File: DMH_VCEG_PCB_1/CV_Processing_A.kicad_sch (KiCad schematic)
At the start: 57 parts, among them Q1 BC558, Q2 BC558, Q3 BC548, Q4 BC548, Q5 BC548, Q6 BC548, U10 TL074, U8 TL074, U9 TL074

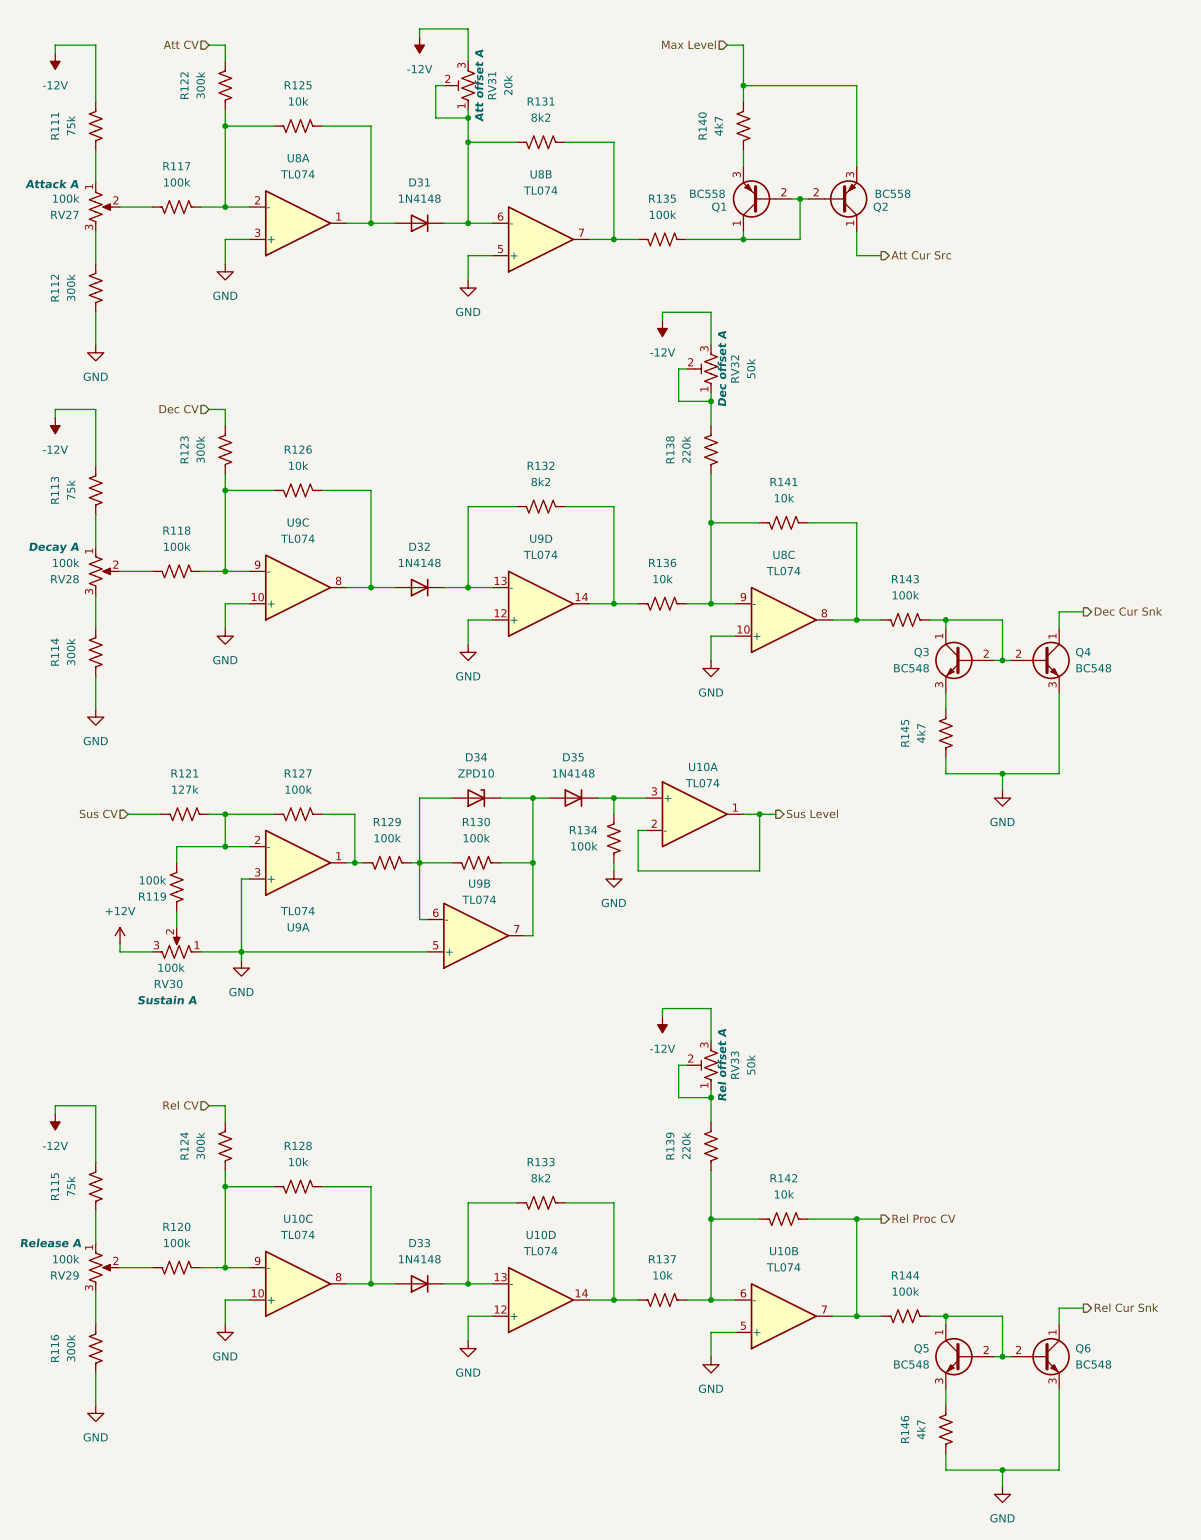
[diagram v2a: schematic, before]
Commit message: Re-annotated whole circuit
Now need to place interface pins and determine in and out of board settings
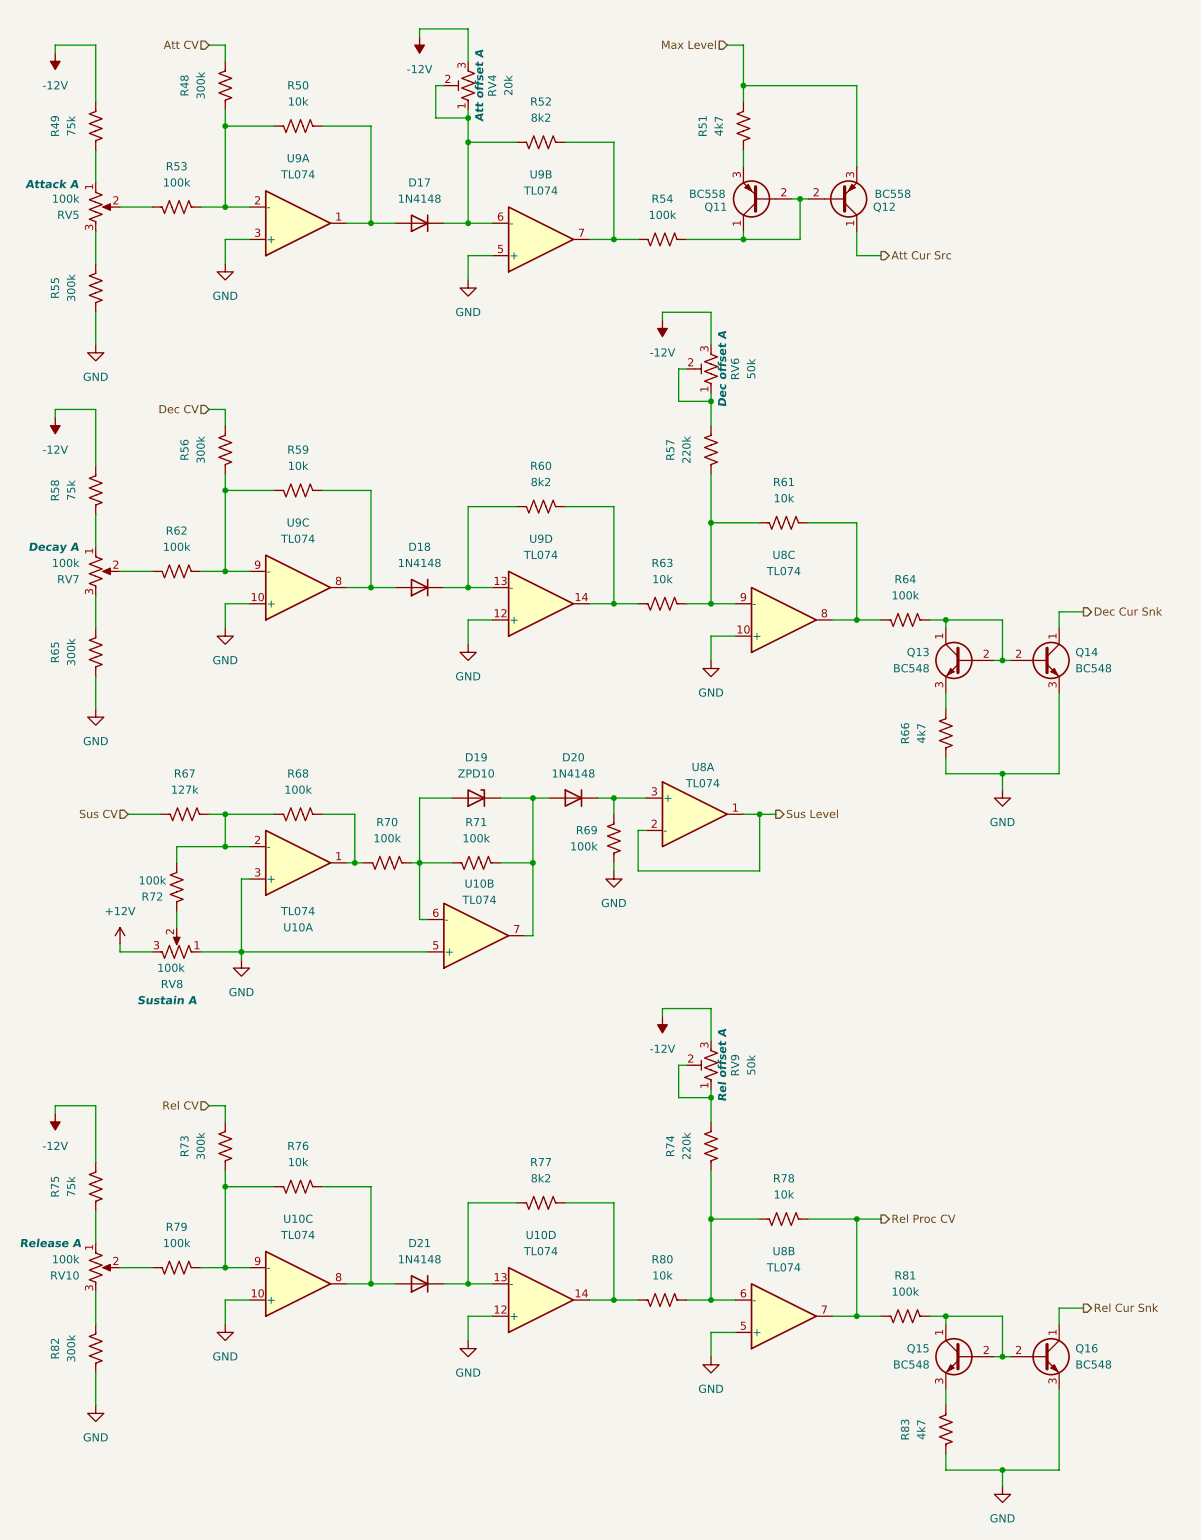
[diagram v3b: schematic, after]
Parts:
- renumbered D31 to D17, D32 to D18, D34 to D19, D35 to D20, D33 to D21, Q1 to Q11, Q2 to Q12, Q3 to Q13, Q4 to Q14, Q5 to Q15, Q6 to Q16, R122 to R48, R111 to R49, R125 to R50, R140 to R51, R131 to R52, R117 to R53, R135 to R54, R112 to R55, R123 to R56, R138 to R57, R113 to R58, R126 to R59, R132 to R60, R141 to R61, R118 to R62, R136 to R63, R143 to R64, R114 to R65, R145 to R66, R121 to R67, R127 to R68, R134 to R69, R129 to R70, R130 to R71, R119 to R72, R124 to R73, R139 to R74, R115 to R75, R128 to R76, R133 to R77, R142 to R78, R120 to R79, R137 to R80, R144 to R81, R116 to R82, R146 to R83, RV29 to RV10, RV31 to RV4, RV27 to RV5, RV32 to RV6, RV28 to RV7, RV30 to RV8, RV33 to RV9, U9 to U10, U10 to U8, U8 to U9

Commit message: Ready for breadboarding
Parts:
- added J22: Conn_01x10_PinHeader, Connector_PinHeader_2.54mm:PinHeader_1x10_P2.54mm_Vertical, symbol SynthStuff:Conn_01x10_PinHeader
- RV4, RV6, RV9: footprint Potentiometer_THT:Potentiometer_Bourns_3296W_Vertical -> Potentiometer_THT:Potentiometer_Bourns_3296X_Horizontal
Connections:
- net Att CV: now also J22.5 (Pin_5)
- net Dec CV: now also J22.6 (Pin_6)
- net Max Level: now also J22.4 (Pin_4)
- net Rel CV: now also J22.8 (Pin_8)
- net Sus CV: now also J22.7 (Pin_7)
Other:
- note added: "PCB 2"

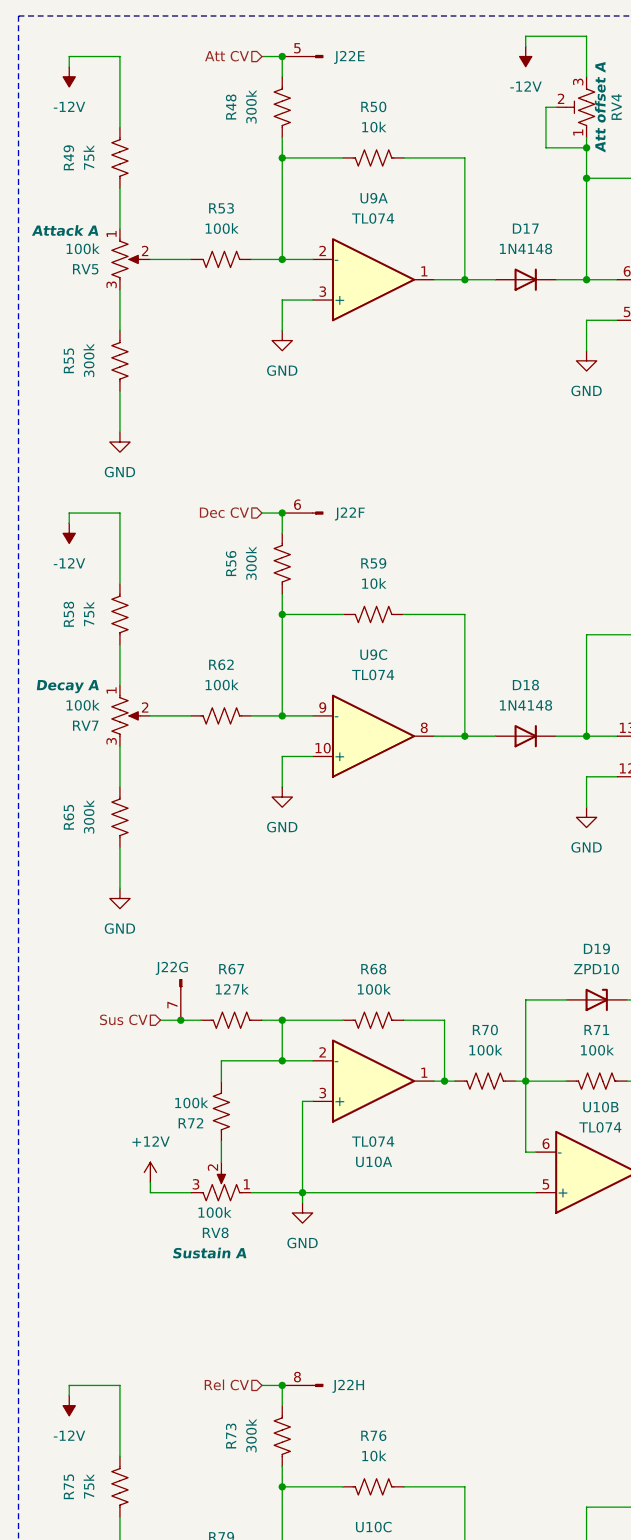
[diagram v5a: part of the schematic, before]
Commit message: PCB 2 placement in progress
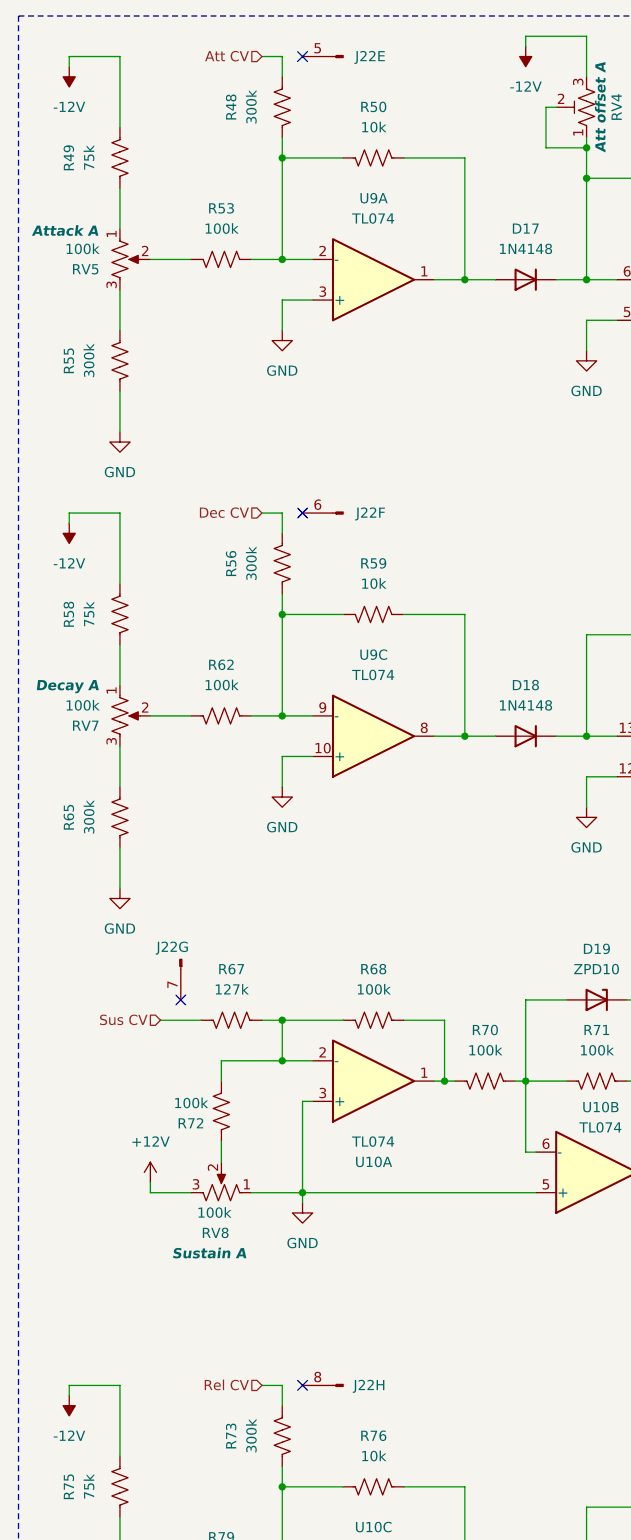
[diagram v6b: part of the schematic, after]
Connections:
- net Att CV: no longer J22.5 (Pin_5)
- net Dec CV: no longer J22.6 (Pin_6)
- net Rel CV: no longer J22.8 (Pin_8)
- net Sus CV: no longer J22.7 (Pin_7)
- no-connect marks 0 -> 4

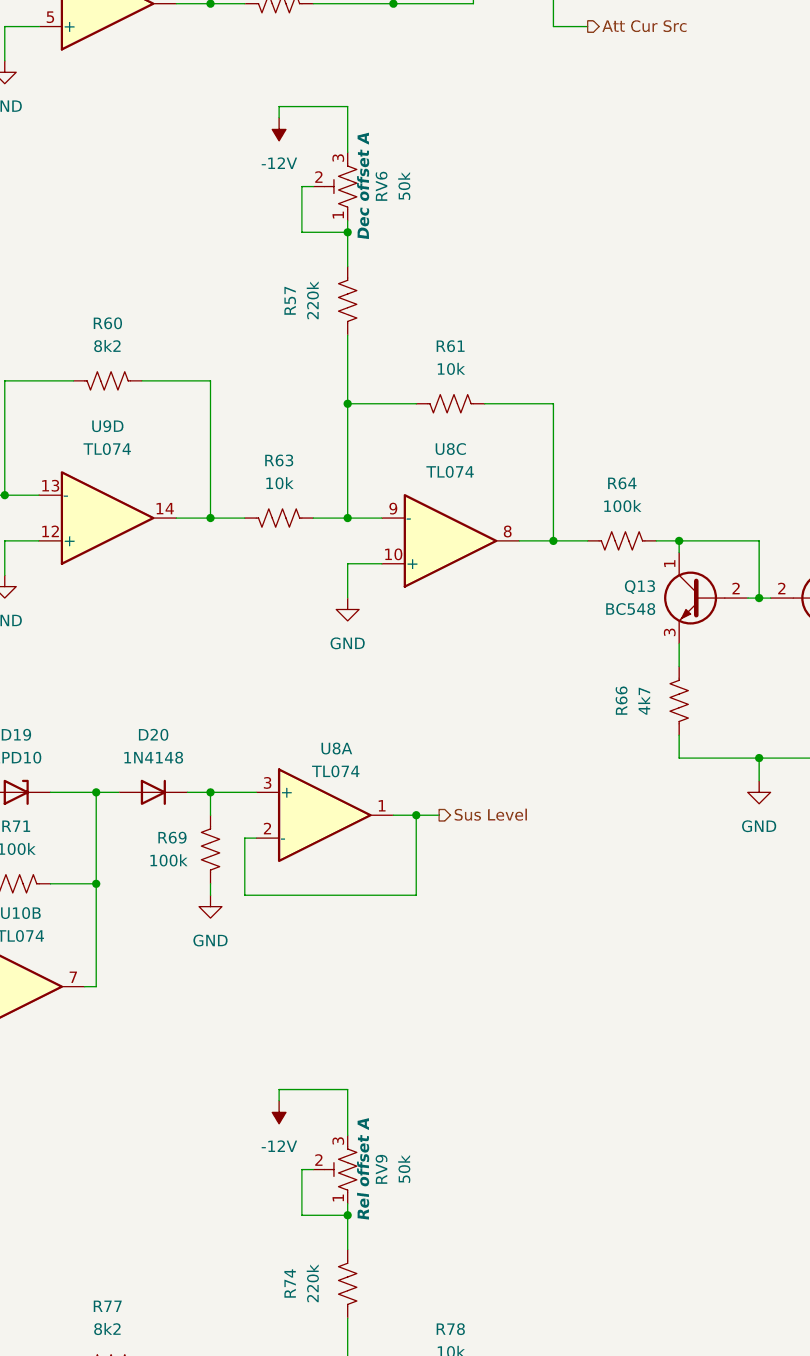
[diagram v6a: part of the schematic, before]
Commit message: Updated Dec and Rel trimpots to 100k
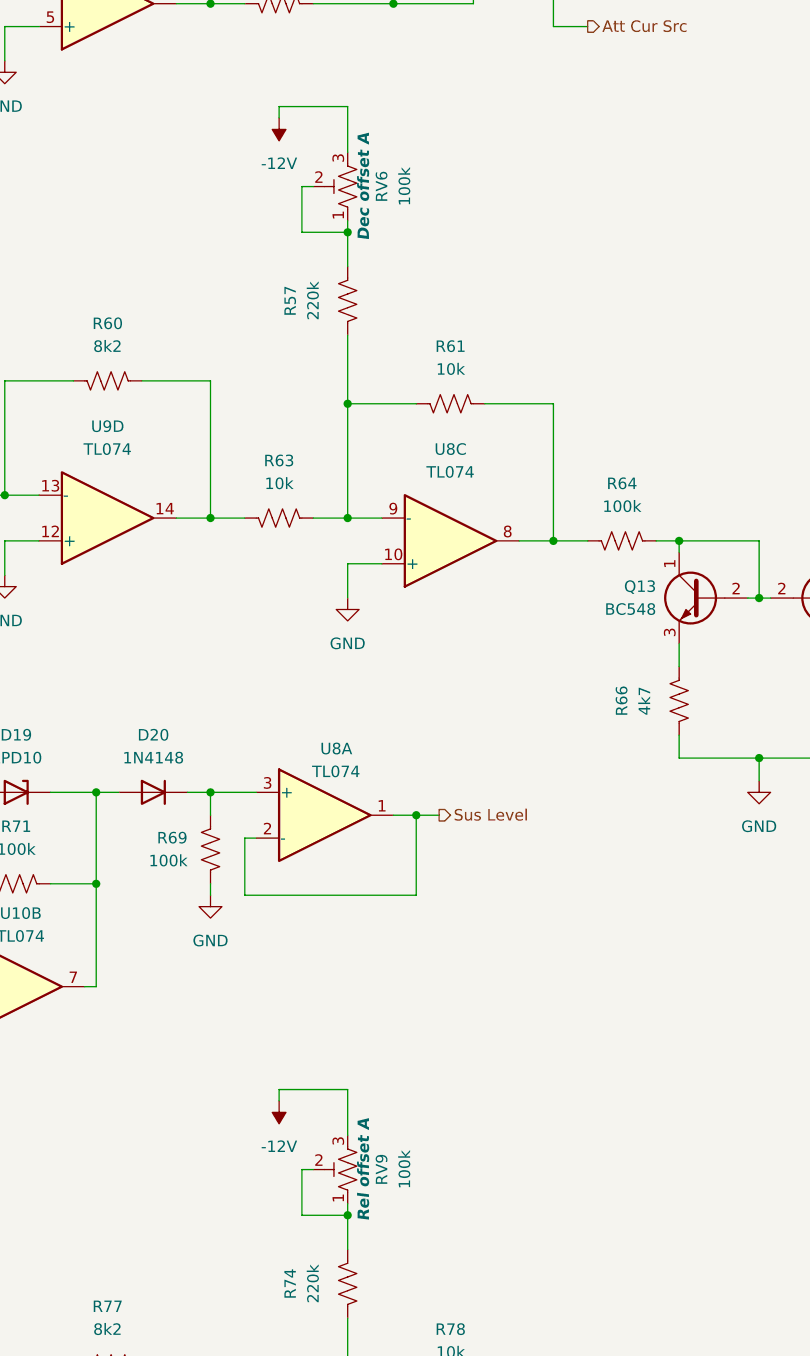
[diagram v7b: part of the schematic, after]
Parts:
- RV6, RV9: value 50k -> 100k
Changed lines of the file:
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@@
 			)
 		)
-		(property "Value" "50k"
+		(property "Value" "100k"
 			(at 128.27 179.07 90)
 			(effects
@@
 			)
 		)
-		(property "Value" "50k"
+		(property "Value" "100k"
 			(at 128.27 69.85 90)
 			(effects

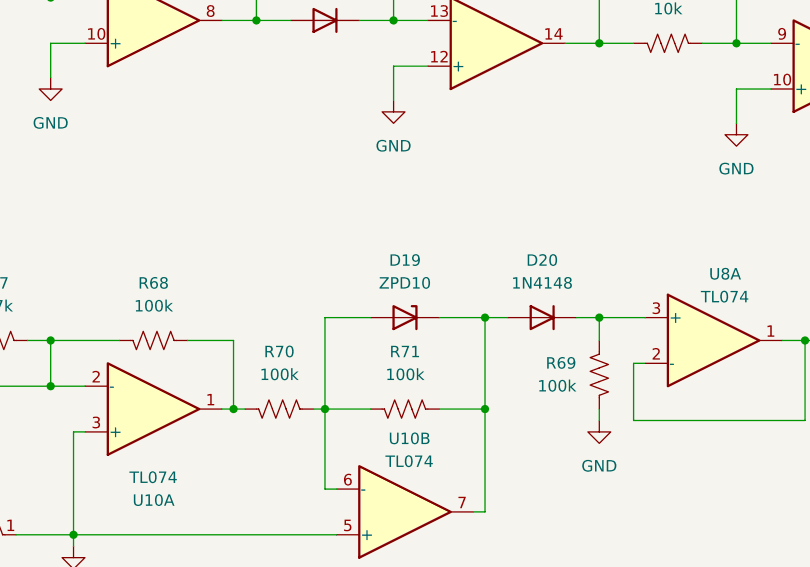
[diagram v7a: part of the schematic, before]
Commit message: PCB 2 placement ongoing
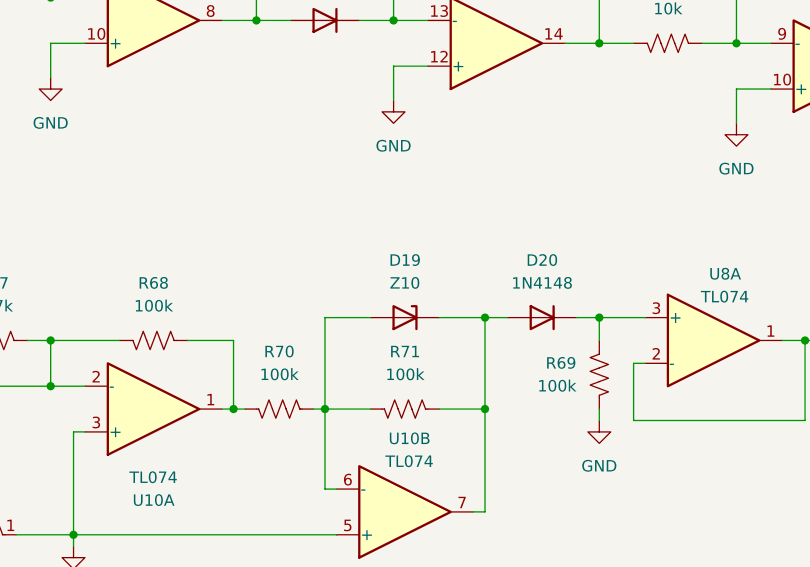
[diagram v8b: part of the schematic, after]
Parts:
- D19: value ZPD10 -> Z10
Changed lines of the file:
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@@
 			)
 		)
-		(property "Value" "ZPD10"
+		(property "Value" "Z10"
 			(at 85.09 133.35 0)
 			(effects
